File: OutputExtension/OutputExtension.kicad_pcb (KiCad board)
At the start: 2 copper layers, 58 x 129 mm, 65 parts, among them P1 CONN_01X04, P2 CONN_01X04, P3 CONN_01X04, P4 CONN_01X08, P5 CONN_01X08, Q1 IRL640, Q10 IRL640, Q11 BSS138, Q12 35N15, Q13 IRL640, Q14 BSS138, Q15 35N15, Q16 IRL640, Q17 BSS138, Q18 35N15, Q19 IRL640, Q2 BSS138, Q20 BSS138, Q21 35N15, Q22 IRL640, Q23 BSS138, Q24 35N15, Q3 35N15, Q4 IRL640, Q5 BSS138, Q6 35N15, Q7 IRL640, Q8 BSS138, Q9 35N15, U1 PCF8574

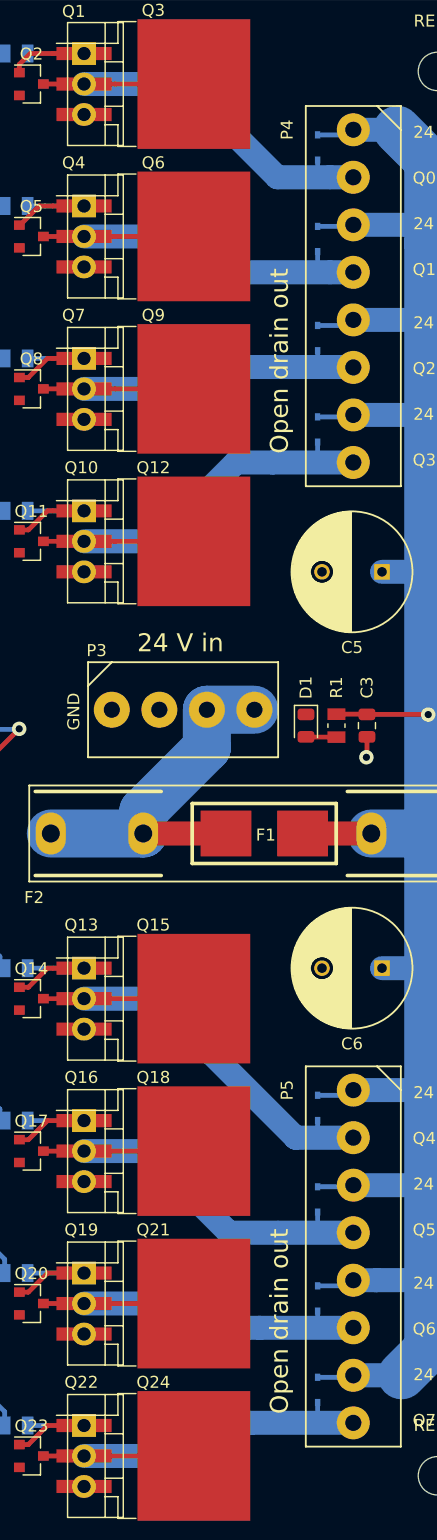
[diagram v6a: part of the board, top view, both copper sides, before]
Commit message: Output extension: chunkier freewheelingdiode
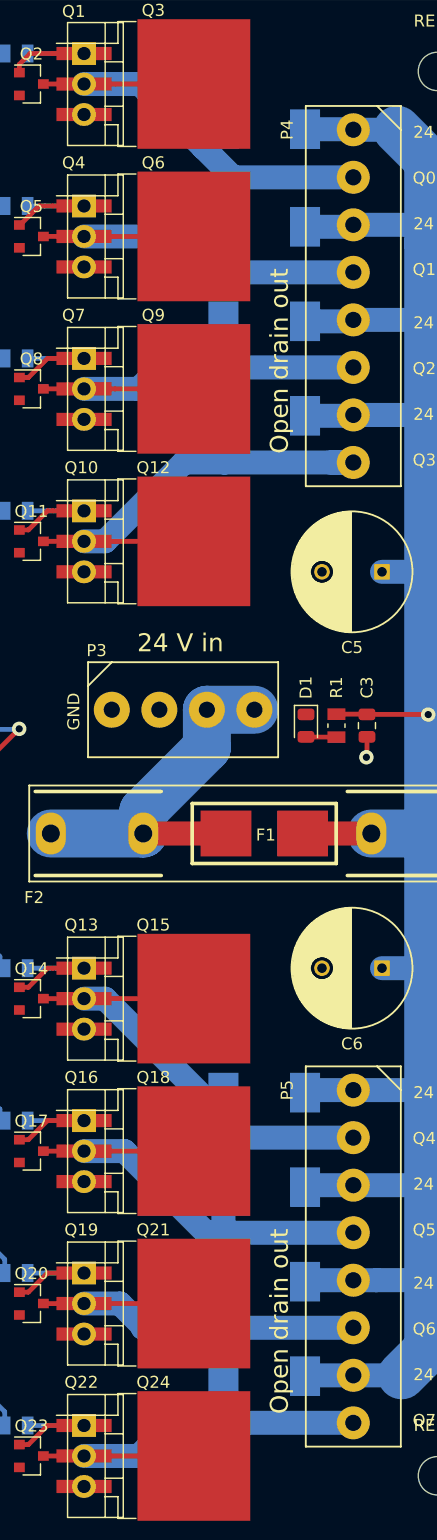
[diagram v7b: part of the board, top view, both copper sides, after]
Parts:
- D10, D3, D4, D5, D6, D7, D8, D9: value B5819WS -> SS310; footprint Diode_SMD:D_SOD-323 -> Diode_SMD:D_SMC
- moved D3 4.70 mm to (115.6, 51.8), turned to 180 degrees
- moved D5 4.66 mm to (115.6, 67.8), turned to 180 degrees
- moved D9 4.66 mm to (115.6, 147.8), turned to 180 degrees
- moved D7 4.62 mm to (115.6, 132.1), turned to 180 degrees
- moved D10 4.59 mm to (115.6, 155.7), turned to 180 degrees
- moved D6 4.59 mm to (115.6, 75.7), turned to 180 degrees
- moved D4 4.56 mm to (115.6, 59.9), turned to 180 degrees
- moved D8 4.56 mm to (115.6, 140.0), turned to 180 degrees
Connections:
- U1 pad 13: Net-(U1-Pad13) -> (no net)
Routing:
- net /powerChannel0/DRAIN: track 65.3 -> 40.5 mm
- net +24V: track 350.4 -> 359.0 mm
- net /powerChannel7/DRAIN: track 46.4 -> 40.0 mm
- net /powerChannel6/DRAIN: track 45.0 -> 39.8 mm
- net /powerChannel5/DRAIN: track 45.8 -> 41.8 mm
- net /powerChannel4/DRAIN: track 45.9 -> 43.0 mm
- net /powerChannel3/DRAIN: track 46.1 -> 43.6 mm
- net /powerChannel1/DRAIN: track 40.9 -> 39.0 mm
